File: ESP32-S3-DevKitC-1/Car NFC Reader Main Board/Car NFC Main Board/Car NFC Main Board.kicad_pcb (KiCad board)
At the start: 2 copper layers, 121.5 x 83.8 mm, 1 part

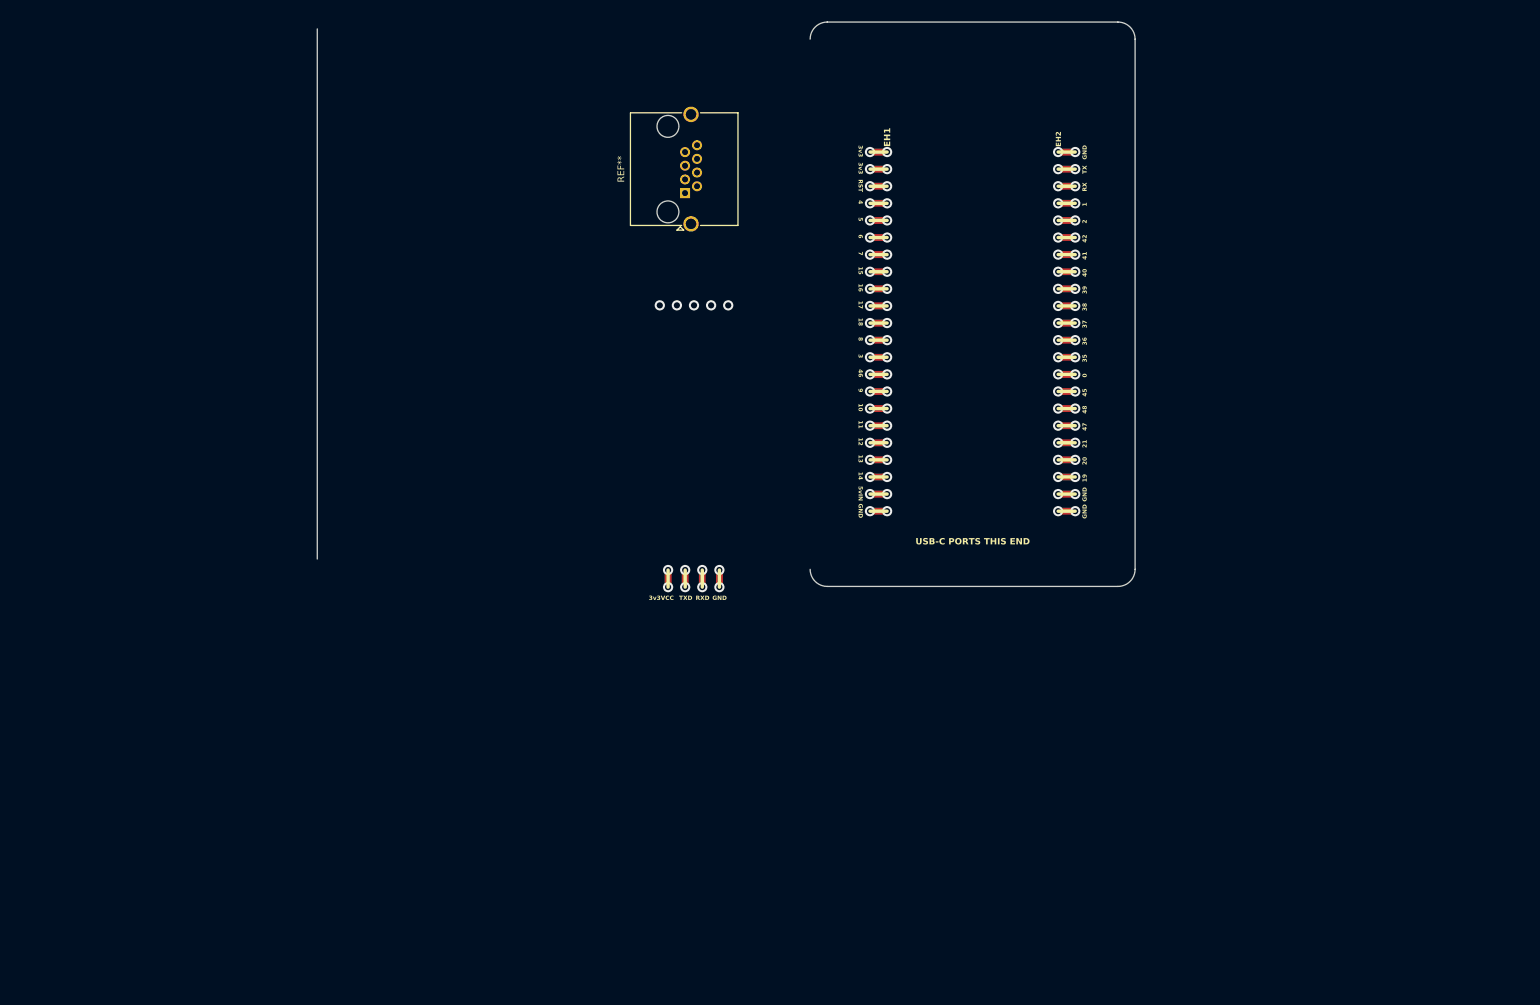
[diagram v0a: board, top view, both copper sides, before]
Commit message: Car NFC proto board as ordered on 2024-06-13
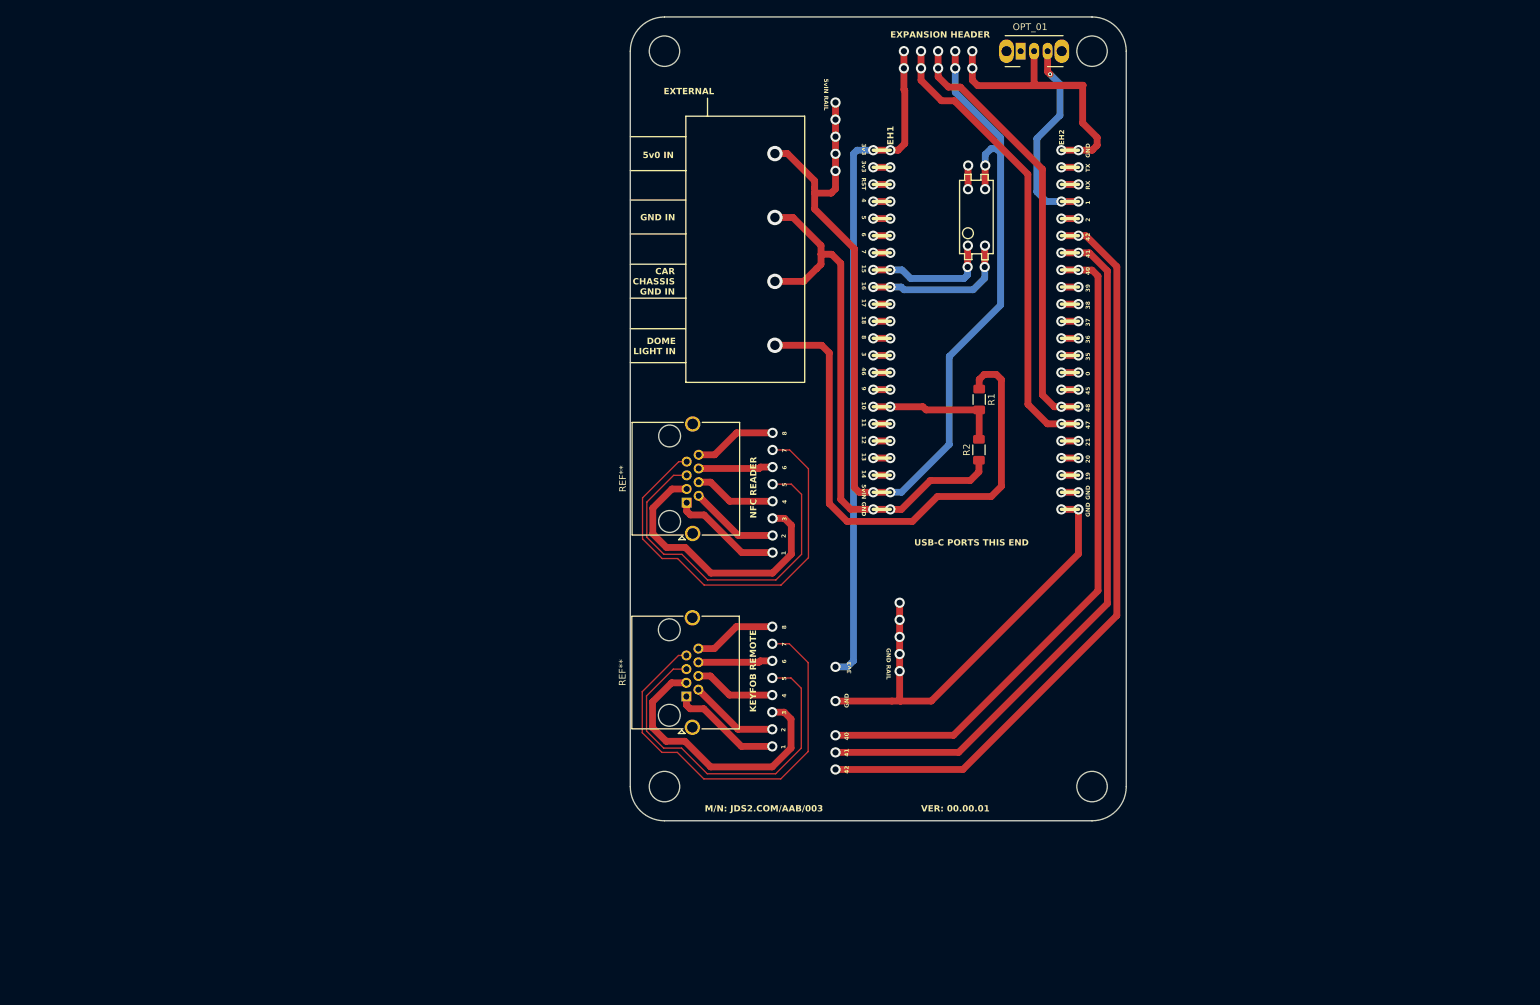
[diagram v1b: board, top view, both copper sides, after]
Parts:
- added OPT_01: SW_Slide_SPDT_Angled_CK_OS102011MA1Q, Button_Switch_THT:SW_Slide_SPDT_Angled_CK_OS102011MA1Q, F.Cu at (177.4, 45.7)
- added R1: 4.7K, Resistor_SMD:R_1206_3216Metric_Pad1.30x1.75mm_HandSolder, F.Cu at (171.2, 97.5)
- added R2: 200R, Resistor_SMD:R_1206_3216Metric_Pad1.30x1.75mm_HandSolder, F.Cu at (171.2, 104.9)
- added REF**: RJ45_Amphenol_RJHSE5380, Connector_RJ:RJ45_Amphenol_RJHSE5380, F.Cu at (127.7, 141.6)
- moved REF** 46.0 mm to (127.8, 112.8)
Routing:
- net (no net): track 121.9 -> 882.6 mm, vias 101 -> 91
- net GND: track 0.00 -> 301.0 mm, vias 0 -> 19
- net 5V0: track 0.00 -> 161.5 mm, vias 0 -> 12
- net TX: track 0.00 -> 97.0 mm, vias 0 -> 9
- net DOME: track 0.00 -> 81.0 mm, vias 0 -> 1
- net RX: track 0.00 -> 71.4 mm, vias 0 -> 6
- net POST_DIVIDER_DOME: track 0.00 -> 20.3 mm, vias 0 -> 2
- net SWITCHED_5V0: track 0.00 -> 3.69 mm, vias 0 -> 2
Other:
- board size 121.5 x 83.8 mm -> 73.7 x 119.4 mm
- board text added: "5v0 IN"
- board text added: "5vIN RAIL"
- board text added: "CAR CHASSIS GND IN"
- board text added: "DOME LIGHT IN"
- board text added: "EXPANSION HEADER"
- board text added: "EXTERNAL"
- board text added: "GND IN"
- board text added: "GND RAIL"
- board text added: "KEYFOB REMOTE"
- board text added: "M/N: JDS2.COM/AAB/003"
- board text added: "NFC READER"
- board text added: "VER: 00.00.01"
- board text removed: "3v3VCC"
- board text removed: "RXD"
- board text removed: "TXD"

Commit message: Fixed tented vias issue
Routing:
- net (no net): vias 91 -> 92
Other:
- rule pad_to_mask_clearance: 0 -> 0.0254
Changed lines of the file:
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@@
 		(48 "B.Fab" user)
 		(49 "F.Fab" user)
-		(50 "User.1" user)
-		(51 "User.2" user)
-		(52 "User.3" user)
-		(53 "User.4" user)
-		(54 "User.5" user)
-		(55 "User.6" user)
-		(56 "User.7" user)
-		(57 "User.8" user)
-		(58 "User.9" user)
 	)
 	(setup
-		(pad_to_mask_clearance 0)
+		(stackup
+			(layer "F.SilkS"
+				(type "Top Silk Screen")
+			)
+			(layer "F.Paste"
+				(type "Top Solder Paste")
+			)
+			(layer "F.Mask"
+				(type "Top Solder Mask")
+				(thickness 0.01)
+			)
+			(layer "F.Cu"
+				(type "copper")
+				(thickness 0.035)
+			)
+			(layer "dielectric 1"
+				(type "core")
+				(thickness 1.51)
+				(material "FR4")
+				(epsilon_r 4.5)
+				(loss_tangent 0.02)
+			)
+			(layer "B.Cu"
+				(type "copper")
+				(thickness 0.035)
+			)
+			(layer "B.Mask"
+				(type "Bottom Solder Mask")
+				(thickness 0.01)
+			)
+			(layer "B.Paste"
+				(type "Bottom Solder Paste")
+			)
+			(layer "B.SilkS"
+				(type "Bottom Silk Screen")
+			)
+			(copper_finish "None")
+			(dielectric_constraints no)
+		)
+		(pad_to_mask_clearance 0.0254)
+		(pad_to_paste_clearance -0.254)
+		(pad_to_paste_clearance_ratio -0.0001)
 		(allow_soldermask_bridges_in_footprints no)
 		(pcbplotparams
@@
 			(svgprecision 4)
 			(plotframeref no)
-			(viasonmask no)
+			(viasonmask yes)
 			(mode 1)
 			(useauxorigin no)
@@
 		(size 1.524)
 		(drill 0.9144)
+		(layers "F.Cu" "B.Cu")
+		(net 0)
+	)
+	(via
+		(at 149.86 134.62)
+		(size 1.524)
+		(drill 0.9144)

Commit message: Final submitted version
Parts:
- added R1: 4.7K, Resistor_SMD:R_1206_3216Metric_Pad1.30x1.75mm_HandSolder, F.Cu at (237.1, 103.0)
- added R2: 200R, Resistor_SMD:R_1206_3216Metric_Pad1.30x1.75mm_HandSolder, F.Cu at (237.1, 110.5)
- added REF**: RJ45_Amphenol_RJHSE5380, Connector_RJ:RJ45_Amphenol_RJHSE5380, F.Cu at (37.8, 111.5)
- added REF**: RJ45_Amphenol_RJHSE5380, Connector_RJ:RJ45_Amphenol_RJHSE5380, F.Cu at (210.3, 103.4)
- added REF**: RJ45_Amphenol_RJHSE5380, Connector_RJ:RJ45_Amphenol_RJHSE5380, F.Cu at (210.3, 123.2)
- added SW_OPT_1: SW_SPDT, Button_Switch_THT:SW_CuK_OS102011MA1QN1_SPDT_Angled, F.Cu at (235.1, 61.3)
- added SW_OPT_2: SW_SPDT, Button_Switch_THT:SW_CuK_OS102011MA1QN1_SPDT_Angled, F.Cu at (248.0, 61.3)
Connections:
- net DOME renamed /DOME
- R1 pad 2: POST_DIVIDER_DOME -> Net-(U1-GPIO10/ADC1_CH9)
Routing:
- net (no net): track 882.6 -> 1127.1 mm, vias 92 -> 159
- net 5V0: track 161.5 -> 0.00 mm, vias 12 -> 0
- net RX: track 71.4 -> 0.00 mm, vias 6 -> 0
- net SWITCHED_5V0: track 3.69 -> 0.00 mm, vias 2 -> 0
- net TX: track 97.0 -> 99.5 mm, vias 9 -> 14
- net GND: track 301.0 -> 303.5 mm, vias 19 -> 27
- net Net-(U1-GPIO10/ADC1_CH9): vias 0 -> 1
- net /DOME: vias 1 -> 2
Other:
- board size 73.7 x 119.4 mm -> 133.1 x 119.9 mm
- board text added: "BLUE"
- board text added: "BROWN"
- board text added: "GREEN"
- board text added: "ORANGE"
- board text added: "VER: 00.01.00"
- board text added: "WHITE/BLUE"
- board text added: "WHITE/BROWN"
- board text added: "WHITE/GREEN"
- board text added: "WHITE/ORANGE"
- board text added: "When hooked up to a normal (commercially made, not crossover) CAT6 cable:"

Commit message: Added ethernet port pinout notes
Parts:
- added REF**: RJ45_Amphenol_RJHSE5380, Connector_RJ:RJ45_Amphenol_RJHSE5380, F.Cu at (38.3, 150.5)
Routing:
- net (no net): track 1127.1 -> 1351.9 mm, vias 159 -> 167
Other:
- board text added: "----BLUE"
- board text added: "----BROWN"
- board text added: "----GREEN"
- board text added: "----ORANGE"
- board text added: "----WHITE/BLUE"
- board text added: "----WHITE/BROWN"
- board text added: "----WHITE/GREEN"
- board text added: "----WHITE/ORANGE"
- board text added: "1: WHITE/ORANGE 2: ORANGE 3: WHITE/GREEN 4: BLUE 5: WHITE/BLUE 6: GREEN 7: WHITE/BROWN 8: BROWN"
- board text added: "Pinout tested on: RJHSE-5380-ND MFG : Amphenol"
- board text added: "RJHSE-5380-ND MFG : Amphenol 1: WHITE/ORANGE 2: ORANGE 3: WHITE/GREEN 4: BLUE 5: WHITE/BLUE 6: GREEN 7: WHITE/BROWN 8: BROWN"
- board text added: "When hooked up to a normal (commercially made, not crossover) CAT6 cable"
- board text removed: "BLUE"
- board text removed: "BROWN"
- board text removed: "GREEN"
- board text removed: "ORANGE"
- board text removed: "WHITE/BLUE"
- board text removed: "WHITE/BROWN"
- board text removed: "WHITE/GREEN"
- board text removed: "WHITE/ORANGE"
- board text removed: "When hooked up to a normal (commercially made, not crossover) CAT6 cable:"
